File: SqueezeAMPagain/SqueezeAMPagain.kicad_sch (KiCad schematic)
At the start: 4 parts

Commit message: Update .gitignore, L_Radial_D12.0mm_P5+6+7.00mm_Fastron_11P.kicad_mod, SqueezeAMPagain.kicad_pcb, and 13 more files
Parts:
- added R27, R28: 10k, Resistor_SMD:R_0603_1608Metric, symbol Device:R
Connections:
- new net +3.3V: R27.1, R28.1
- new net SCL: R27.2
- new net SDA: R28.2
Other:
- sheet DisplayConnector renamed FPConnector
- added sheet USB-Uart (USB-Uart.kicad_sch)
- sheet FPConnector ports: added IO1, IO2, IO3, IO4, SCL, SDA, ~{WAKE}; removed none
- sheet Pico ports: added BCLK, DATA, LRCLK, MCLK, RX, SCL, SDA, SPI0_CS, SPI0_MISO, SPI0_MOSI, SPI0_SCK, TX; removed none
- sheet Power ports: added LV_ON, PON, ~{WAKE_DETECT}, ~{WAKE}; removed none
- sheet esp ports: added GPIO0/BOOT/I2S0_MCLK, I2S0_SCLK, I2S0_SD, I2S0_WCLK, IO12, IO13, IO15, IO27; removed GPIO0/BOOT, I2S-CLK, I2S-SD, I2S-WS, IO22, SPDIF_OUT
- moved on the sheet: H1, H2, H3, H4

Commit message: Update SqueezeAMPagain.kicad_pcb, SqueezeAMPagain.kicad_sch, USB-Uart.kicad_sch, and 4 more files
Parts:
- R27, R28: JLCPCB# (none) -> C25804
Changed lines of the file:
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@@
+			)
+		)
+		(property "JLCPCB#" "C25804"
+			(at 255.27 24.13 0)
+			(effects
+				(font
+					(size 1.27 1.27)
+				)
+				(hide yes)
 			)
 		)
@@
 			(at 275.59 24.13 0)
 			(effects
+				(font
+					(size 1.27 1.27)
+				)
+				(hide yes)
+			)
+		)
+		(property "JLCPCB#" "C25804"
+			(at 275.59 24.13 0)
+			(effects

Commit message: Update SqueezeAMPagain.kicad_pcb, SqueezeAMPagain.kicad_prl, SqueezeAMPagain.kicad_pro, and 6 more files
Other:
- added sheet X_PSU (X_PSU.kicad_sch)
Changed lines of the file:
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@@
+	)
+	(junction
+		(at 57.15 171.45)
+		(diameter 0)
+		(color 0 0 0 0)
+	)
+	(junction
+		(at 71.12 168.91)
+		(diameter 0)
+		(color 0 0 0 0)
 	)
 	(junction
@@
 	)
 	(junction
+		(at 74.93 166.37)
+		(diameter 0)
+		(color 0 0 0 0)
+	)
+	(junction
 		(at 173.99 81.28)
 		(diameter 0)
@@
 	(wire
 		(pts
-			(xy 120.65 177.8) (xy 120.65 110.49)
+			(xy 120.65 168.91) (xy 120.65 110.49)
 		)
 		(stroke
@@
 	(wire
 		(pts
-			(xy 104.14 177.8) (xy 120.65 177.8)
+			(xy 106.68 168.91) (xy 120.65 168.91)
 		)
 		(stroke
@@
 	(wire
 		(pts
-			(xy 78.74 175.26) (xy 74.93 175.26)
+			(xy 81.28 166.37) (xy 74.93 166.37)
 		)
 		(stroke
@@
 	(wire
 		(pts
-			(xy 57.15 114.3) (xy 57.15 180.34)
+			(xy 57.15 114.3) (xy 57.15 171.45)
+		)
+		(stroke
+			(width 0)
+			(type default)
+		)
+	)
+	(wire
+		(pts
+			(xy 74.93 184.15) (xy 74.93 166.37)
 		)
 		(stroke
@@
 	(wire
 		(pts
-			(xy 57.15 180.34) (xy 78.74 180.34)
+			(xy 57.15 171.45) (xy 81.28 171.45)
 		)
 		(stroke
@@
 	(wire
 		(pts
+			(xy 81.28 189.23) (xy 57.15 189.23)
+		)
+		(stroke
+			(width 0)
+			(type default)
+		)
+	)
+	(wire
+		(pts
 			(xy 68.58 27.94) (xy 68.58 80.01)
 		)
@@
 	(wire
 		(pts
+			(xy 81.28 186.69) (xy 71.12 186.69)
+		)
+		(stroke
+			(width 0)
+			(type default)
+		)
+	)
+	(wire
+		(pts
 			(xy 50.8 100.33) (xy 129.54 100.33)
 		)
@@
 	(wire
 		(pts
+			(xy 71.12 186.69) (xy 71.12 168.91)
+		)
+		(stroke
+			(width 0)
+			(type default)
+		)
+	)
+	(wire
+		(pts
 			(xy 176.53 78.74) (xy 195.58 78.74)
 		)
@@
 	(wire
 		(pts
+			(xy 57.15 189.23) (xy 57.15 171.45)
+		)
+		(stroke
+			(width 0)
+			(type default)
+		)
+	)
+	(wire
+		(pts
 			(xy 173.99 41.91) (xy 173.99 81.28)
 		)
@@
 	(wire
 		(pts
-			(xy 74.93 107.95) (xy 74.93 175.26)
+			(xy 81.28 184.15) (xy 74.93 184.15)
+		)
+		(stroke
+			(width 0)
+			(type default)
+		)
+	)
+	(wire
+		(pts
+			(xy 74.93 107.95) (xy 74.93 166.37)
 		)
 		(stroke
@@
 	(wire
 		(pts
-			(xy 78.74 177.8) (xy 71.12 177.8)
+			(xy 81.28 168.91) (xy 71.12 168.91)
 		)
 		(stroke
@@
 	(wire
 		(pts
-			(xy 71.12 177.8) (xy 71.12 105.41)
+			(xy 71.12 168.91) (xy 71.12 105.41)
 		)
 		(stroke
@@
 	)
 	(sheet
-		(at 78.74 170.18)
+		(at 81.28 161.29)
 		(size 25.4 13.97)
 		(fields_autoplaced yes)
@@
 		)
 		(property "Sheetname" "Power"
-			(at 78.74 169.4684 0)
+			(at 81.28 160.5784 0)
 			(effects
 				(font
@@
 		)
 		(property "Sheetfile" "power.kicad_sch"
-			(at 78.74 184.7346 0)
+			(at 81.28 175.8446 0)
 			(effects
 				(font
@@
 		)
 		(pin "PON" input
-			(at 78.74 175.26 180)
+			(at 81.28 166.37 180)
 			(effects
 				(font
@@
 		)
 		(pin "LV_ON" input
-			(at 78.74 177.8 180)
+			(at 81.28 168.91 180)
 			(effects
 				(font
@@
 		)
 		(pin "~{WAKE}" input
-			(at 78.74 180.34 180)
+			(at 81.28 171.45 180)
 			(effects
 				(font
@@
 		)
 		(pin "~{WAKE_DETECT}" output
-			(at 104.14 177.8 0)
+			(at 106.68 168.91 0)
 			(effects
 				(font
@@
 				)
 			)
+		)
+	)
+	(sheet
+		(at 81.28 180.34)
+		(size 25.4 12.7)
+		(fields_autoplaced yes)
+		(stroke
+			(width 0.1524)
+			(type solid)
+		)
+		(fill
+			(color 0 0 0 0.0000)
+		)
+		(property "Sheetname" "X_PSU"
+			(at 81.28 179.6284 0)
+			(effects
+				(font
+					(size 1.27 1.27)
+				)
+				(justify left bottom)
+			)
+		)
+		(property "Sheetfile" "X_PSU.kicad_sch"
+			(at 81.28 193.6246 0)
+			(effects
+				(font
+					(size 1.27 1.27)
+				)
+				(justify left top)
+			)
+		)
+		(pin "PON" input
+			(at 81.28 184.15 180)
+			(effects
+				(font
+					(size 1.27 1.27)
+				)
+				(justify left)
+			)
+		)
+		(pin "LV_ON" input
+			(at 81.28 186.69 180)
+			(effects
+				(font
+					(size 1.27 1.27)
+				)
+				(justify left)
+			)
+		)
+		(pin "~{WAKE}" input
+			(at 81.28 189.23 180)
+			(effects
+				(font
+					(size 1.27 1.27)
+				)
+				(justify left)
+			)
+		)
+		(instances
+			(project "SqueezeAMPagain"
+				(path "/3675160b-d9e5-490e-b506-2a7966e79ed0"
+					(page "14")
+				)
+			)

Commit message: Update SqueezeAMPagain.kicad_pcb, SqueezeAMPagain.kicad_prl, SqueezeAMPagain.kicad_pro, and 7 more files
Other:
- sheet Pi ports: added BCLK, DATA, LRCLK, PWM, SCL, SDA; removed none
- sheet Pico ports: added GPIO10, GPIO11, GPIO18, GPIO19, GPIO20, GPIO6, GPIO7, GPIO8, GPIO9; removed none
- sheet X_PSU ports: added SCL, SDA; removed none
- moved on the sheet: H1, H2, H3, H4

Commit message: Update L_Radial_D12.0mm_P5+6+7.00mm_Fastron_11P.kicad_mod, SqueezeAMPagain.kicad_pcb, SqueezeAMPagain.kicad_prl, and 5 more files
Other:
- sheet Pi ports: added GPIO25, MISO, MOSI, SCLK, ~{CE0}; removed none

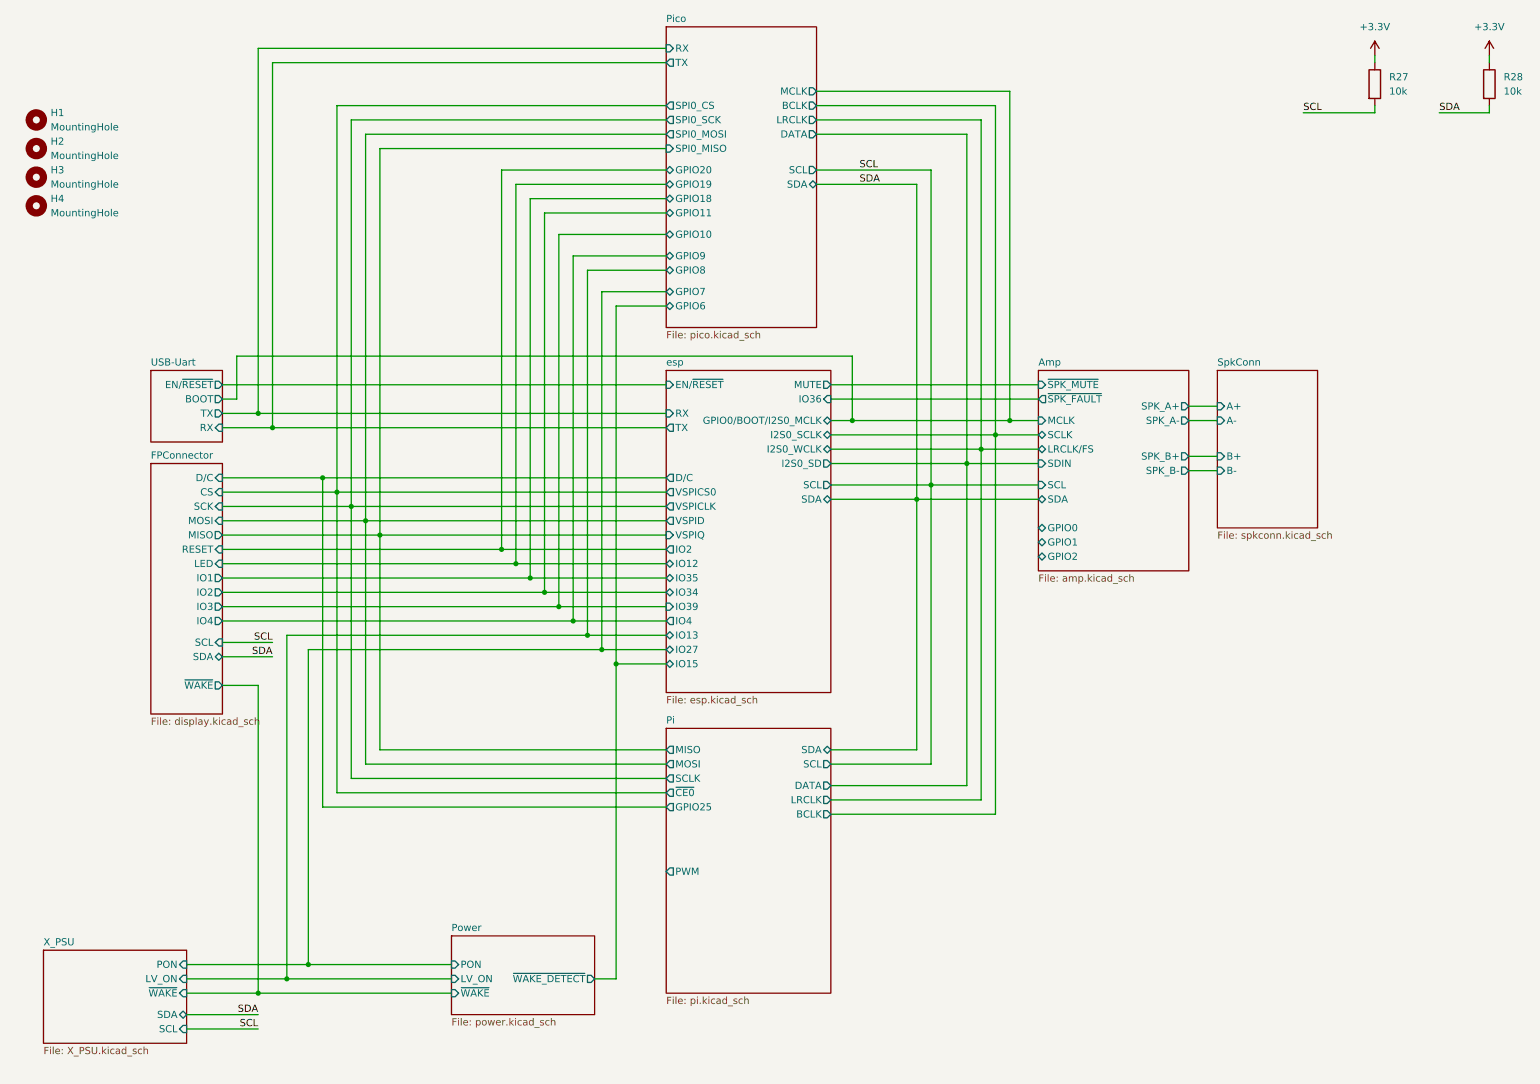
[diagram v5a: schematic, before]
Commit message: Update SqueezeAMPagain.kicad_pcb, SqueezeAMPagain.kicad_prl, SqueezeAMPagain.kicad_pro, and 5 more files
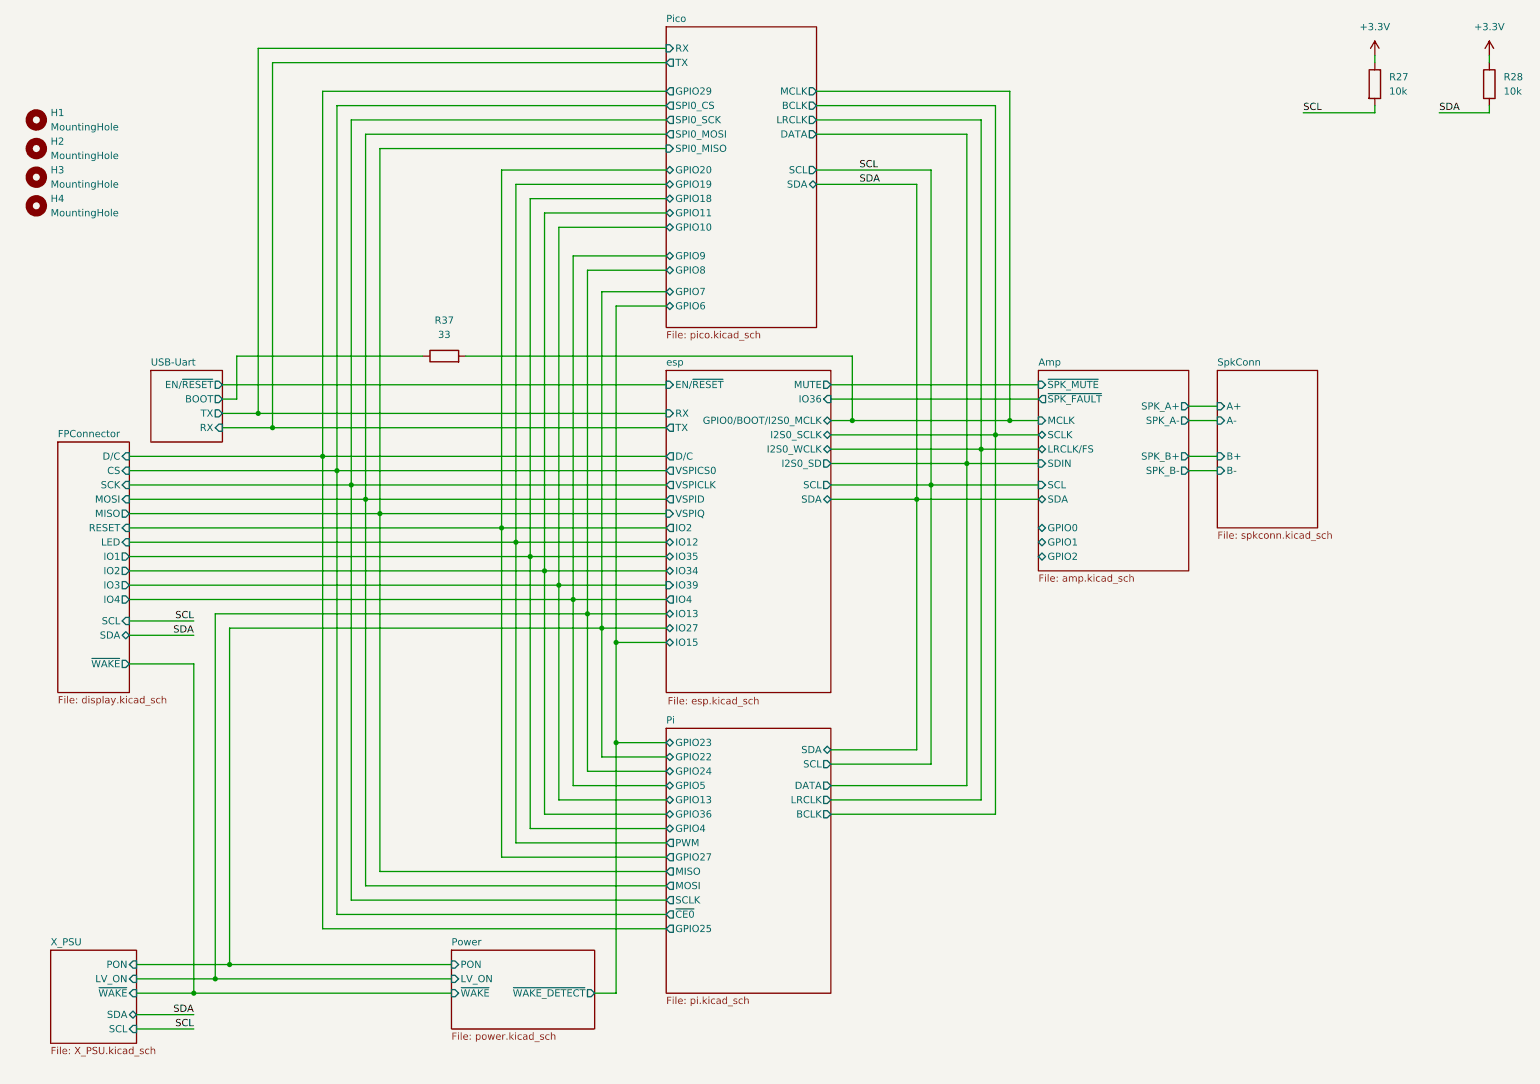
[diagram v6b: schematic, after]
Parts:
- added R37: 33, Resistor_SMD:R_0402_1005Metric, symbol Device:R
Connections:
- net Amp/MCLK: now also R37.2
- new net USB-Uart/BOOT: R37.1
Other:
- sheet Pi ports: added GPIO13, GPIO22, GPIO23, GPIO24, GPIO27, GPIO36, GPIO4, GPIO5; removed none
- sheet Pico ports: added GPIO29; removed none

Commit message: Update SqueezeAMPagain.kicad_pcb, SqueezeAMPagain.kicad_prl, SqueezeAMPagain.kicad_pro, and 11 more files
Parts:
- renumbered R37 to R1, R27 to R2, R28 to R3
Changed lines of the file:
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@@
 		(dnp no)
 		(fields_autoplaced yes)
-		(property "Reference" "#PWR095"
+		(property "Reference" "#PWR02"
 			(at 275.59 22.86 0)
 			(effects
@@
 			(project "SqueezeAMPagain"
 				(path "/3675160b-d9e5-490e-b506-2a7966e79ed0"
-					(reference "#PWR095")
+					(reference "#PWR02")
 					(unit 1)
 				)
@@
 		(dnp no)
 		(fields_autoplaced yes)
-		(property "Reference" "R37"
+		(property "Reference" "R1"
 			(at 90.17 66.04 90)
 			(effects
@@
 			(project "SqueezeAMPagain"
 				(path "/3675160b-d9e5-490e-b506-2a7966e79ed0"
-					(reference "R37")
+					(reference "R1")
 					(unit 1)
 				)
@@
 		(on_board yes)
 		(dnp no)
-		(property "Reference" "R27"
+		(property "Reference" "R2"
 			(at 257.81 22.8599 0)
 			(effects
@@
 			(project "SqueezeAMPagain"
 				(path "/3675160b-d9e5-490e-b506-2a7966e79ed0"
-					(reference "R27")
+					(reference "R2")
 					(unit 1)
 				)
@@
 		(dnp no)
 		(fields_autoplaced yes)
-		(property "Reference" "#PWR094"
+		(property "Reference" "#PWR01"
 			(at 255.27 22.86 0)
 			(effects
@@
 			(project "SqueezeAMPagain"
 				(path "/3675160b-d9e5-490e-b506-2a7966e79ed0"
-					(reference "#PWR094")
+					(reference "#PWR01")
 					(unit 1)
 				)
@@
 		(on_board yes)
 		(dnp no)
-		(property "Reference" "R28"
+		(property "Reference" "R3"
 			(at 278.13 22.8599 0)
 			(effects
@@
 			(project "SqueezeAMPagain"
 				(path "/3675160b-d9e5-490e-b506-2a7966e79ed0"
-					(reference "R28")
-					(unit 1)
-				)
+					(reference "R3")
+					(unit 1)
+				)

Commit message: Update SqueezeAMPagain.kicad_pcb, SqueezeAMPagain.kicad_prl, SqueezeAMPagain.kicad_pro, and 4 more files
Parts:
- added H5: MountingHole, MountingHole:MountingHole_2.5mm, symbol Mechanical:MountingHole
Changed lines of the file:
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@@
+	)
+	(symbol
+		(lib_id "Mechanical:MountingHole")
+		(at 17.78 59.69 0)
+		(unit 1)
+		(exclude_from_sim yes)
+		(in_bom no)
+		(on_board yes)
+		(dnp no)
+		(property "Reference" "H5"
+			(at 20.32 58.4199 0)
+			(effects
+				(font
+					(size 1.27 1.27)
+				)
+				(justify left)
+			)
+		)
+		(property "Value" "MountingHole"
+			(at 20.32 60.9599 0)
+			(effects
+				(font
+					(size 1.27 1.27)
+				)
+				(justify left)
+			)
+		)
+		(property "Footprint" "MountingHole:MountingHole_2.5mm"
+			(at 17.78 59.69 0)
+			(effects
+				(font
+					(size 1.27 1.27)
+				)
+				(hide yes)
+			)
+		)
+		(property "Datasheet" "~"
+			(at 17.78 59.69 0)
+			(effects
+				(font
+					(size 1.27 1.27)
+				)
+				(hide yes)
+			)
+		)
+		(property "Description" "Mounting Hole without connection"
+			(at 17.78 59.69 0)
+			(effects
+				(font
+					(size 1.27 1.27)
+				)
+				(hide yes)
+			)
+		)
+		(instances
+			(project "SqueezeAMPagain"
+				(path "/3675160b-d9e5-490e-b506-2a7966e79ed0"
+					(reference "H5")
+					(unit 1)
+				)
+			)
+		)
 	)
 	(symbol
